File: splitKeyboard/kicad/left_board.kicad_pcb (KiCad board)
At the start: 2 copper layers, 305 x 136.1 mm, 126 parts

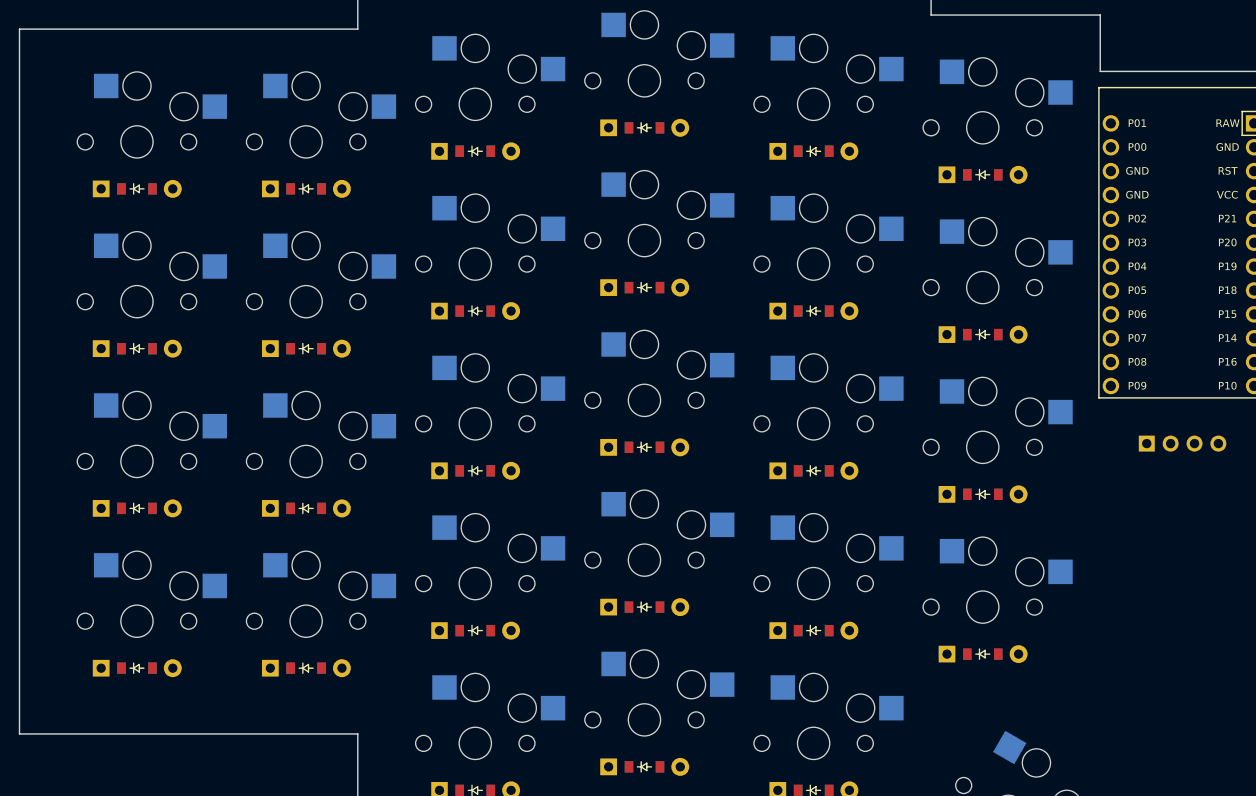
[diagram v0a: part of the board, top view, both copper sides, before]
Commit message: feat(board): mounting points and case
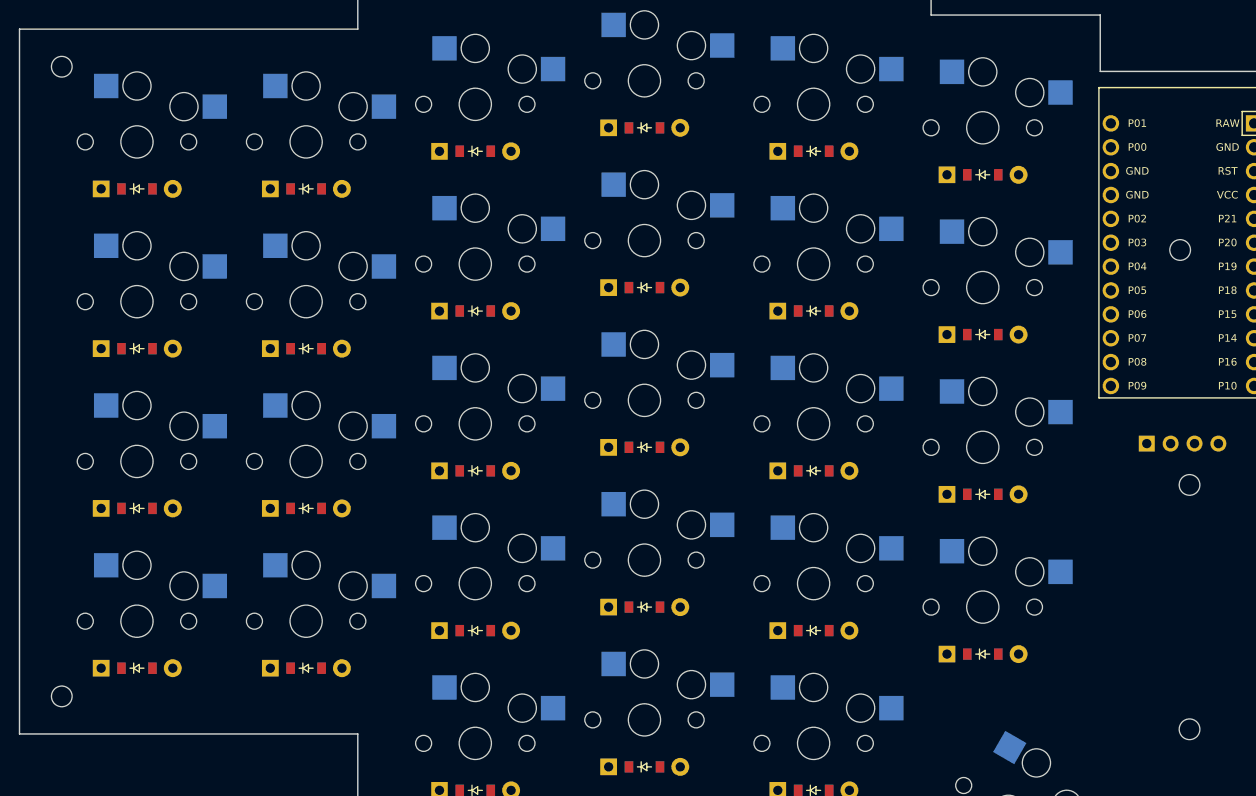
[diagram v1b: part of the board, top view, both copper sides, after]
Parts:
- added MH1: , ceoloide:mounting_hole_npth, F.Cu at (92.0, 24.0)
- added MH2: , ceoloide:mounting_hole_npth, F.Cu at (92.0, 91.0)
- added MH3: , ceoloide:mounting_hole_npth, F.Cu at (212.0, 94.5)
- added MH4: , ceoloide:mounting_hole_npth, F.Cu at (212.0, 68.5)
- added MH5: , ceoloide:mounting_hole_npth, F.Cu at (211.0, 43.5)
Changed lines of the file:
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@@
         (pad 2 thru_hole circle (at 3.81 0 90) (size 1.905 1.905) (drill 0.9906) (layers *.Cu *.Mask) (net 78 "VCC"))
     )
+  (footprint "ceoloide:mounting_hole_npth"
+    (layer "F.Cu")
+    (at 92 24 0)
+    (property "Reference" "MH1"
+      (at 0 2.55 0)
+      (layer "F.SilkS")
+      hide
+      (effects (font (size 1 1) (thickness 0.15)))
+    )
+    (pad "" np_thru_hole circle
+      (at 0 0 0)
+      (size 2.2 2.2)
+      (drill 2.2)
+      (layers "*.Cu" "*.Mask")
+    )
+  )
+  (footprint "ceoloide:mounting_hole_npth"
+    (layer "F.Cu")
+    (at 92 91 0)
+    (property "Reference" "MH2"
+      (at 0 2.55 0)
+      (layer "F.SilkS")
+      hide
+      (effects (font (size 1 1) (thickness 0.15)))
+    )
+    (pad "" np_thru_hole circle
+      (at 0 0 0)
+      (size 2.2 2.2)
+      (drill 2.2)
+      (layers "*.Cu" "*.Mask")
+    )
+  )
+  (footprint "ceoloide:mounting_hole_npth"
+    (layer "F.Cu")
+    (at 212 94.5 0)
+    (property "Reference" "MH3"
+      (at 0 2.55 0)
+      (layer "F.SilkS")
+      hide
+      (effects (font (size 1 1) (thickness 0.15)))
+    )
+    (pad "" np_thru_hole circle
+      (at 0 0 0)
+      (size 2.2 2.2)
+      (drill 2.2)
+      (layers "*.Cu" "*.Mask")
+    )
+  )
+  (footprint "ceoloide:mounting_hole_npth"
+    (layer "F.Cu")
+    (at 212 68.5 0)
+    (property "Reference" "MH4"
+      (at 0 2.55 0)
+      (layer "F.SilkS")
+      hide
+      (effects (font (size 1 1) (thickness 0.15)))
+    )
+    (pad "" np_thru_hole circle
+      (at 0 0 0)
+      (size 2.2 2.2)
+      (drill 2.2)
+      (layers "*.Cu" "*.Mask")
+    )
+  )
+  (footprint "ceoloide:mounting_hole_npth"
+    (layer "F.Cu")
+    (at 211 43.5 0)
+    (property "Reference" "MH5"
+      (at 0 2.55 0)
+      (layer "F.SilkS")
+      hide
+      (effects (font (size 1 1) (thickness 0.15)))
+    )
+    (pad "" np_thru_hole circle
+      (at 0 0 0)
+      (size 2.2 2.2)
+      (drill 2.2)
+      (layers "*.Cu" "*.Mask")
+    )
+  )
   (gr_line (start 87.5 95) (end 123.5 95) (layer Edge.Cuts) (stroke (width 0.15) (type default)))
 (gr_line (start 87.5 95) (end 87.5 20) (layer Edge.Cuts) (stroke (width 0.15) (type default)))

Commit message: fix: got rid of unnecessary extra side
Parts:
- removed D33, D34, D35, D36, D37, D38, D39, D40, D41, D42, D43, D44, D45, D46, D47, D48, D49, D50, D51, D52, D53, D54, D55, D56, D57, D58, D59, D60, D61, D62: , ComboDiode
- removed S31, S32, S33, S34, S35, S36, S37, S38, S39, S40, S41, S42, S43, S44, S45, S46, S47, S48, S49, S50, S51, S52, S53, S54, S55, S56, S57, S58, S59, S60: , PG1350
- moved D32 158.5 mm to (223.8, 44.5), turned to 90 degrees
- moved D31 158.3 mm to (227.8, 44.5), turned to 90 degrees
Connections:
- D31 pad 1: P7 -> GND
- D31 pad 2: mirror_outer_bottom -> P0
- D32 pad 1: P6 -> GND
- D32 pad 2: mirror_outer_home -> VCC
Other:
- board size 305 x 136.1 mm -> 148.6 x 136.1 mm

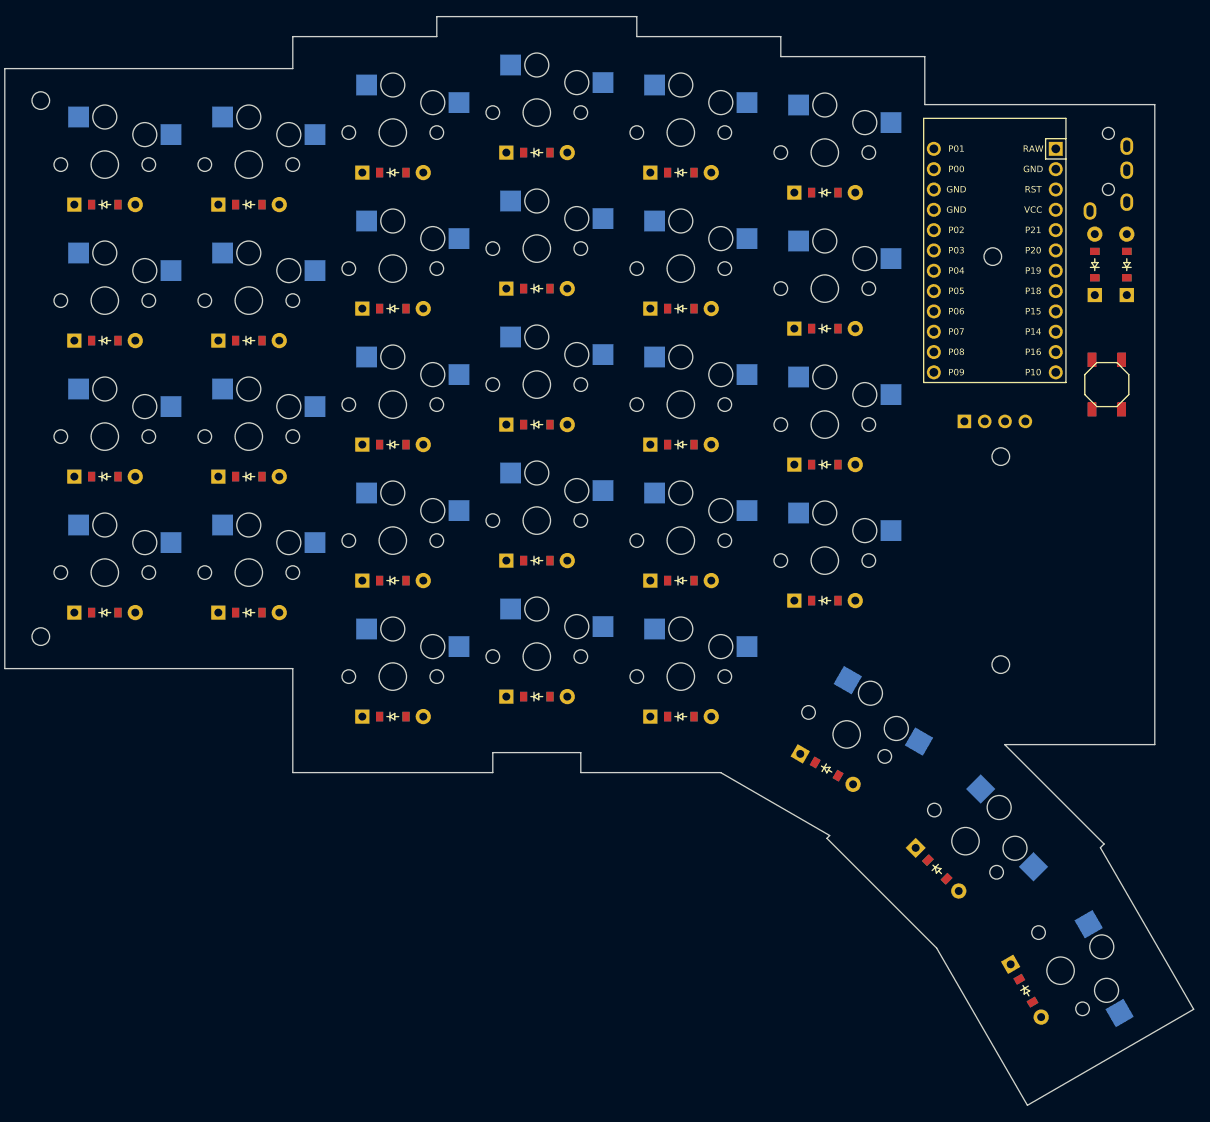
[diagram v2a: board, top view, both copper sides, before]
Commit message: feat(left_board): left_board traced
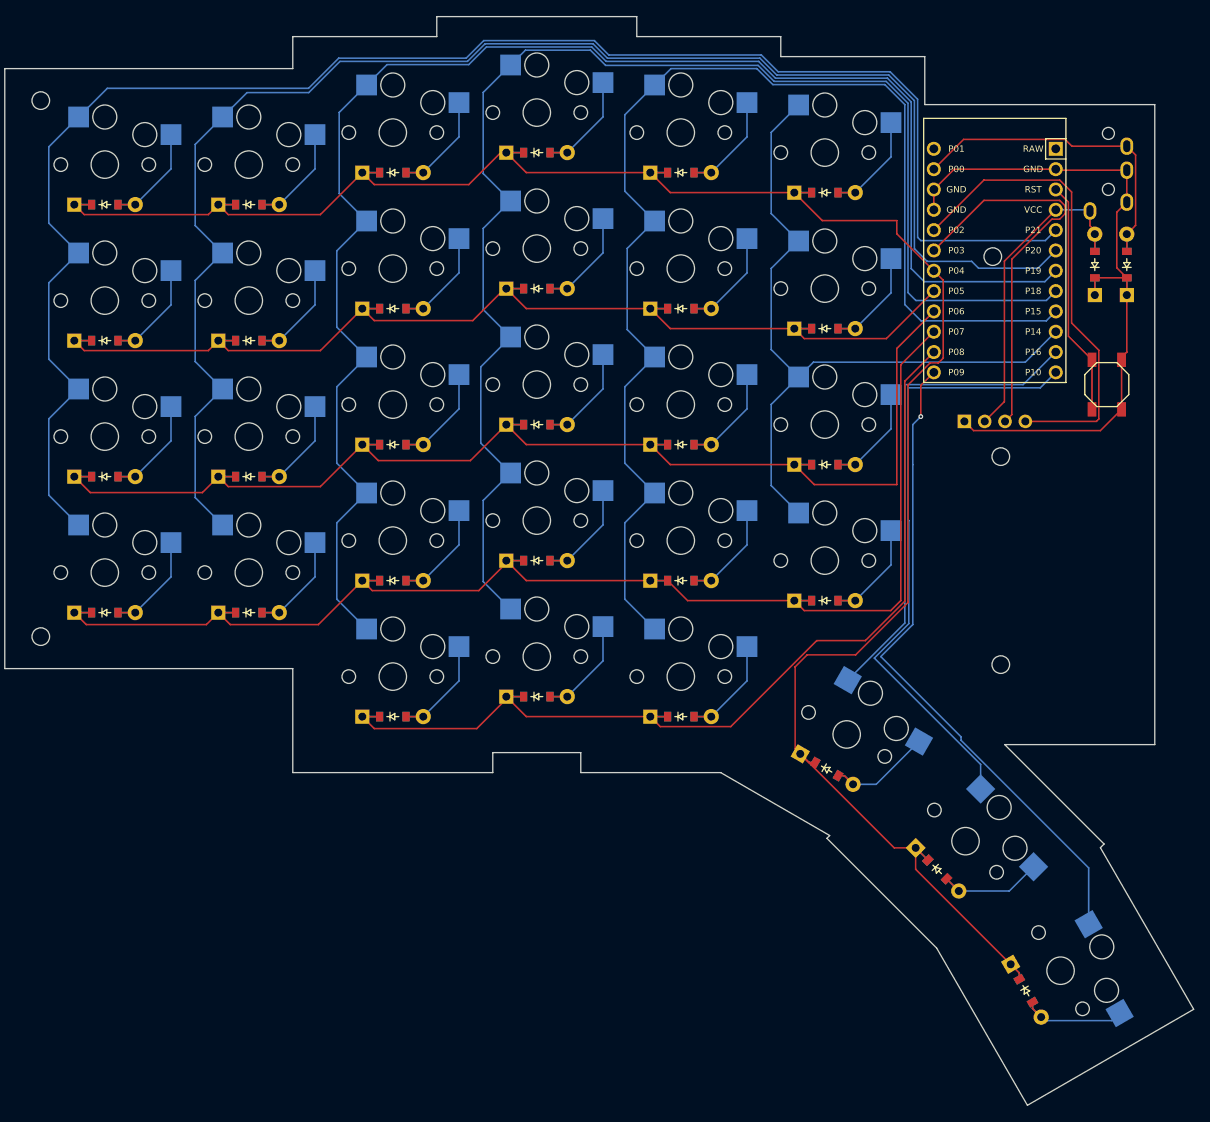
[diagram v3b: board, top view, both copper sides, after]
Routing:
- net P4: track 0.00 -> 271.8 mm
- net P21: track 0.00 -> 207.4 mm
- net P19: track 0.00 -> 193.1 mm
- net P20: track 0.00 -> 190.8 mm
- net P18: track 0.00 -> 175.8 mm
- net P7: track 0.00 -> 171.9 mm
- net P6: track 0.00 -> 162.4 mm
- net P15: track 0.00 -> 159.3 mm
- net P5: track 0.00 -> 144.4 mm
- net P8: track 0.00 -> 123.9 mm
- net P14: track 0.00 -> 94.0 mm
- net GND: track 0.00 -> 90.7 mm
- net P9: track 0.00 -> 82.5 mm, vias 0 -> 1
- net P10: track 0.00 -> 76.7 mm
- net P16: track 0.00 -> 60.5 mm
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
